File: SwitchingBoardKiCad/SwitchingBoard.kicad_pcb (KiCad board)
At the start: 2 copper layers, 100 x 74.5 mm, 53 parts, among them J1 Screw_Terminal_01x02, J2 Screw_Terminal_01x02, J3 Screw_Terminal_01x02, J4 Screw_Terminal_01x02, J5 Screw_Terminal_01x02, J6 Screw_Terminal_01x03, J7 Screw_Terminal_01x02, J8 Screw_Terminal_01x02, J9 Screw_Terminal_01x02, K1 FINDER-30.22, Q1 BT169G, Q2 BTB16-800CW, Q3 BTB16-800CW

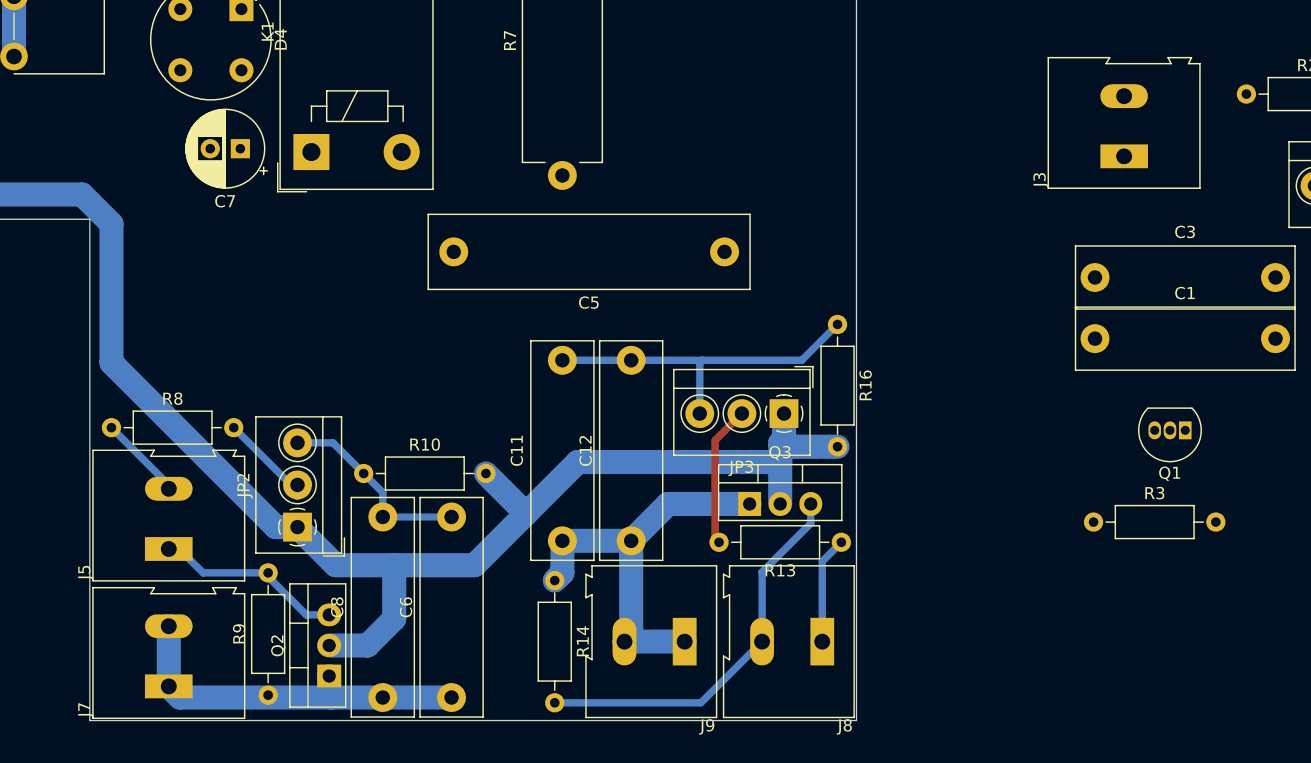
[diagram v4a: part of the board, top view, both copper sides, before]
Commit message: Fixed TRIAC symbol and tweaked layout further.
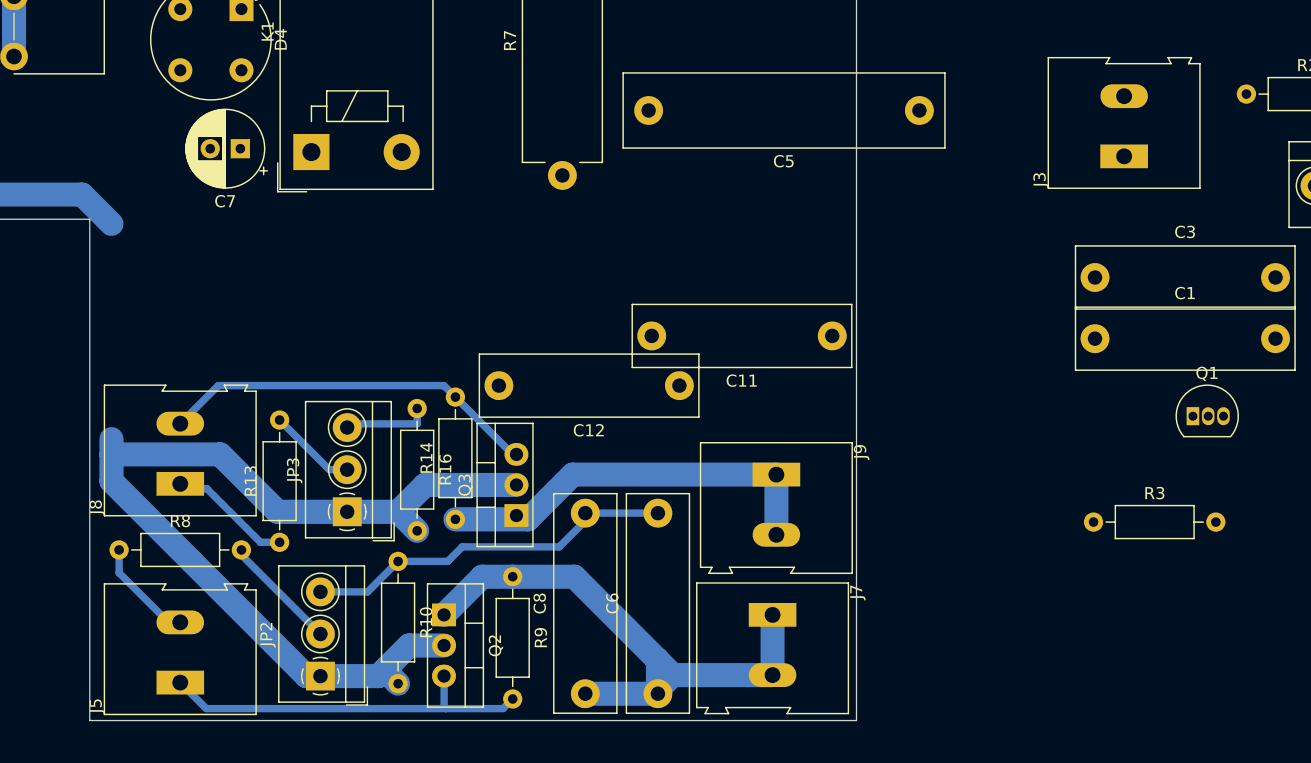
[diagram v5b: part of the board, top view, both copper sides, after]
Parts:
- Q1: value BT169G -> Q_TRIAC_A2GA1; footprint Package_TO_SOT_THT:TO-92_Inline -> Package_TO_SOT_THT:TO-92L_Inline
- moved J8 54.9 mm to (75.8, 80.2), turned to 90 degrees
- moved J7 50.5 mm to (125.0, 91.1), turned to -90 degrees
- moved R13 46.7 mm to (84.1, 85.1), turned to 90 degrees
- moved JP3 37.2 mm to (89.7, 82.6), turned to 90 degrees
- moved R16 35.6 mm to (95.5, 74.0)
- moved C11 28.2 mm to (130.0, 67.9), turned to 180 degrees
- moved R9 22.6 mm to (103.4, 87.9), turned to -90 degrees
- moved C5 20.0 mm to (137.2, 49.2)
- moved Q3 19.4 mm to (103.7, 82.9), turned to 90 degrees
- moved C6 17.1 mm to (115.5, 97.7)
- moved C8 16.8 mm to (109.5, 97.7)
- moved J9 15.8 mm to (125.3, 79.5), turned to -90 degrees
- moved C12 13.5 mm to (117.3, 72.1), turned to 180 degrees
- moved JP2 12.5 mm to (87.5, 96.2)
- moved J5 11.1 mm to (75.8, 96.7)
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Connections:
- J8 pad 1: Net-(R13-Pad1) -> Net-(J8-Pad1)
- J8 pad 2: Net-(Q3-Pad3) -> Net-(J8-Pad2)
- Q3 pad 3: Net-(Q3-Pad3) -> Net-(J8-Pad1)
- R13 pad 1: Net-(R13-Pad1) -> Net-(J8-Pad2)
- R14 pad 2: Net-(Q3-Pad3) -> Net-(J8-Pad1)
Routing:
- net Net-(J8-Pad1): track 0.00 -> 41.9 mm
- net Net-(Q3-Pad3): track 32.4 -> 0.00 mm
- net /Live: track 153.5 -> 127.4 mm
- net Net-(C11-Pad2): track 28.6 -> 7.21 mm
- net /Inrush protection: track 31.0 -> 48.1 mm
- net Net-(J5-Pad1): track 16.3 -> 31.6 mm
- net Net-(C6-Pad2): track 16.5 -> 31.1 mm
- net Net-(R13-Pad1): track 8.91 -> 0.00 mm
- net Net-(JP3-Pad2): track 11.7 -> 7.32 mm
- net Net-(JP2-Pad2): track 7.91 -> 9.71 mm
- net Net-(J5-Pad2): track 7.05 -> 8.71 mm
- net /Protection short: track 34.0 -> 33.2 mm
